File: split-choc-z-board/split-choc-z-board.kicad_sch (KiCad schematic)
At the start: 44 parts, among them J1 AudioJack4_Ground, SW1 SW_SPST, SW10 SW_SPST, SW11 SW_SPST, SW12 SW_SPST, SW13 SW_SPST, SW14 SW_SPST, SW15 SW_SPST, SW16 SW_SPST, SW17 SW_SPST, SW18 SW_SPST, SW2 SW_SPST, SW3 SW_SPST, SW4 SW_SPST, SW5 SW_SPST, SW6 SW_SPST, SW7 SW_SPST, SW8 SW_SPST, SW9 SW_SPST

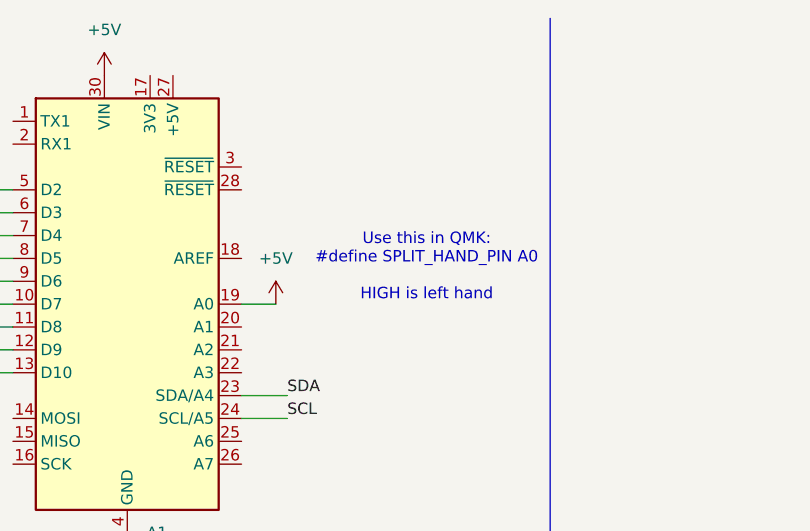
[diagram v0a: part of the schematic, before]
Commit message: Refactored schematic and added footprint library
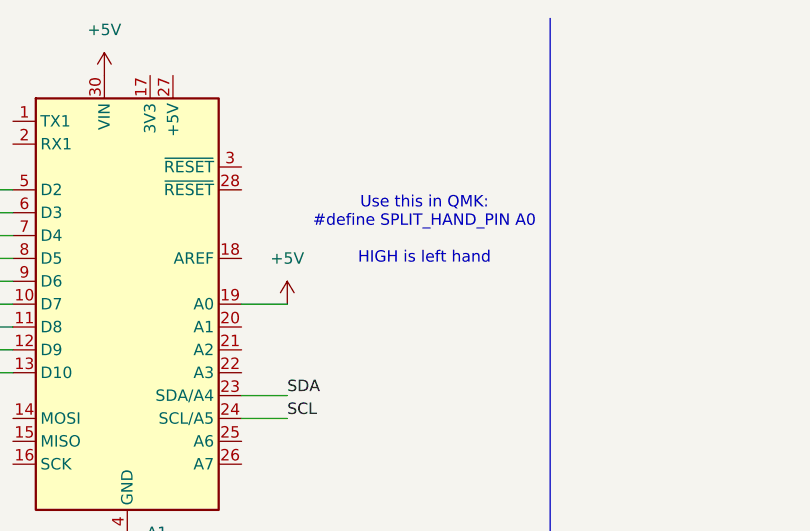
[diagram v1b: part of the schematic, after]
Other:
- title: (none) -> Split Choc Z Board Master Layout
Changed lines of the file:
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@@
 	(generator_version "9.0")
 	(paper "A4")
+	(title_block
+		(title "Split Choc Z Board Master Layout")
+		(date "2025-05-07")
+		(rev "1")
+	)
 	(text "Use this in QMK: \n#define SPLIT_HAND_PIN A0\n\nHIGH is left hand"
 		(exclude_from_sim no)
-		(at 113.284 40.386 0)
+		(at 113.03 36.322 0)
 		(effects
 			(font
@@
 	(wire
 		(pts
-			(xy 92.71 44.45) (xy 96.52 44.45)
-		)
-		(stroke
-			(width 0)
-			(type default)
-		)
-	)
-	(wire
-		(pts
 			(xy 64.77 44.45) (xy 67.31 44.45)
 		)
@@
 	(wire
 		(pts
+			(xy 92.71 44.45) (xy 97.79 44.45)
+		)
+		(stroke
+			(width 0)
+			(type default)
+		)
+	)
+	(wire
+		(pts
 			(xy 231.14 139.7) (xy 205.74 139.7)
 		)
@@
 	(symbol
 		(lib_id "power:+5V")
-		(at 96.52 44.45 0)
+		(at 97.79 44.45 0)
 		(unit 1)
 		(exclude_from_sim no)
@@
 		(dnp no)
 		(fields_autoplaced yes)
-		(property "Reference" "#PWR012"
-			(at 96.52 48.26 0)
+		(property "Reference" "#PWR014"
+			(at 97.79 48.26 0)
 			(effects
 				(font
@@
 		)
 		(property "Value" "+5V"
-			(at 96.52 39.37 0)
+			(at 97.79 39.37 0)
 			(effects
 				(font
@@
 		)
 		(property "Footprint" ""
-			(at 96.52 44.45 0)
+			(at 97.79 44.45 0)
 			(effects
 				(font
@@
 		)
 		(property "Datasheet" ""
-			(at 96.52 44.45 0)
+			(at 97.79 44.45 0)
 			(effects
 				(font
@@
 		)
 		(property "Description" "Power symbol creates a global label with name \"+5V\""
-			(at 96.52 44.45 0)
+			(at 97.79 44.45 0)
 			(effects
 				(font
@@
 			(project "split-choc-z-board"
 				(path "/ed5781c6-5e97-451b-a423-3f437c76b176"
-					(reference "#PWR012")
+					(reference "#PWR014")
 					(unit 1)
 				)

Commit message: Added more footprints to symbols and started placement
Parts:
- D1, D10, D11, D12, D13, D14, D15, D16, D17, D18, D2, D3, D4, D5, D6, D7, D8, D9: footprint (none) -> Diode_THT:D_DO-35_SOD27_P7.62mm_Horizontal
- R1, R2, R3, R4, R5, R6: footprint (none) -> Resistor_THT:R_Axial_DIN0207_L6.3mm_D2.5mm_P10.16mm_Horizontal
- SW1, SW10, SW11, SW12, SW13, SW14, SW15, SW16, SW17, SW18, SW2, SW3, SW4, SW5, SW6, SW7, SW8, SW9: footprint (none) -> ScottoKeebs_Choc:Choc_V2_1.00u
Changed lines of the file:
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@@
 			)
 		)
-		(property "Footprint" ""
+		(property "Footprint" "Resistor_THT:R_Axial_DIN0207_L6.3mm_D2.5mm_P10.16mm_Horizontal"
 			(at 221.742 34.29 90)
 			(effects
@@
 			)
 		)
-		(property "Footprint" ""
+		(property "Footprint" "ScottoKeebs_Choc:Choc_V2_1.00u"
 			(at 269.24 78.74 0)
 			(effects
@@
 			)
 		)
-		(property "Footprint" ""
+		(property "Footprint" "Diode_THT:D_DO-35_SOD27_P7.62mm_Horizontal"
 			(at 260.35 78.74 0)
 			(effects
@@
 			)
 		)
-		(property "Footprint" ""
+		(property "Footprint" "ScottoKeebs_Choc:Choc_V2_1.00u"
 			(at 218.44 53.34 0)
 			(effects
@@
 			)
 		)
-		(property "Footprint" ""
+		(property "Footprint" "ScottoKeebs_Choc:Choc_V2_1.00u"
 			(at 243.84 78.74 0)
 			(effects
@@
 			)
 		)
-		(property "Footprint" ""
+		(property "Footprint" "Diode_THT:D_DO-35_SOD27_P7.62mm_Horizontal"
 			(at 234.95 78.74 0)
 			(effects
@@
 			)
 		)
-		(property "Footprint" ""
+		(property "Footprint" "ScottoKeebs_Choc:Choc_V2_1.00u"
 			(at 243.84 154.94 0)
 			(effects
@@
 			)
 		)
-		(property "Footprint" ""
+		(property "Footprint" "ScottoKeebs_Choc:Choc_V2_1.00u"
 			(at 218.44 154.94 0)
 			(effects
@@
 			)
 		)
-		(property "Footprint" ""
+		(property "Footprint" "ScottoKeebs_Choc:Choc_V2_1.00u"
 			(at 193.04 53.34 0)
 			(effects
@@
 			)
 		)
-		(property "Footprint" ""
+		(property "Footprint" "Resistor_THT:R_Axial_DIN0207_L6.3mm_D2.5mm_P10.16mm_Horizontal"
 			(at 39.37 25.908 90)
 			(effects
@@
 			)
 		)
-		(property "Footprint" ""
+		(property "Footprint" "ScottoKeebs_Choc:Choc_V2_1.00u"
 			(at 269.24 129.54 0)
 			(effects
@@
 			)
 		)
-		(property "Footprint" ""
+		(property "Footprint" "ScottoKeebs_Choc:Choc_V2_1.00u"
 			(at 218.44 78.74 0)
 			(effects
@@
 			)
 		)
-		(property "Footprint" ""
+		(property "Footprint" "ScottoKeebs_Choc:Choc_V2_1.00u"
 			(at 193.04 78.74 0)
 			(effects
@@
 			)
 		)
-		(property "Footprint" ""
+		(property "Footprint" "Diode_THT:D_DO-35_SOD27_P7.62mm_Horizontal"
 			(at 260.35 104.14 0)
 			(effects
@@
 			)
 		)
-		(property "Footprint" ""
+		(property "Footprint" "Diode_THT:D_DO-35_SOD27_P7.62mm_Horizontal"
 			(at 209.55 104.14 0)
 			(effects
@@
 			)
 		)
-		(property "Footprint" ""
+		(property "Footprint" "ScottoKeebs_Choc:Choc_V2_1.00u"
 			(at 269.24 53.34 0)
 			(effects
@@
 			)
 		)
-		(property "Footprint" ""
+		(property "Footprint" "ScottoKeebs_Choc:Choc_V2_1.00u"
 			(at 243.84 53.34 0)
 			(effects
@@
 			)
 		)
-		(property "Footprint" ""
+		(property "Footprint" "Diode_THT:D_DO-35_SOD27_P7.62mm_Horizontal"
 			(at 184.15 53.34 0)
 			(effects
@@
 			)
 		)
-		(property "Footprint" ""
+		(property "Footprint" "Diode_THT:D_DO-35_SOD27_P7.62mm_Horizontal"
 			(at 260.35 53.34 0)
 			(effects
@@
 			)
 		)
-		(property "Footprint" ""
+		(property "Footprint" "Diode_THT:D_DO-35_SOD27_P7.62mm_Horizontal"
 			(at 234.95 154.94 0)
 			(effects
@@
 			)
 		)
-		(property "Footprint" ""
+		(property "Footprint" "ScottoKeebs_Choc:Choc_V2_1.00u"
 			(at 269.24 104.14 0)
 			(effects
@@
 			)
 		)
-		(property "Footprint" ""
+		(property "Footprint" "Diode_THT:D_DO-35_SOD27_P7.62mm_Horizontal"
 			(at 260.35 129.54 0)
 			(effects
@@
 			)
 		)
-		(property "Footprint" ""
+		(property "Footprint" "Resistor_THT:R_Axial_DIN0207_L6.3mm_D2.5mm_P10.16mm_Horizontal"
 			(at 196.342 34.29 90)
 			(effects
@@
 			)
 		)
-		(property "Footprint" ""
+		(property "Footprint" "Diode_THT:D_DO-35_SOD27_P7.62mm_Horizontal"
 			(at 184.15 129.54 0)
 			(effects
@@
 			)
 		)
-		(property "Footprint" ""
+		(property "Footprint" "Diode_THT:D_DO-35_SOD27_P7.62mm_Horizontal"
 			(at 209.55 53.34 0)
 			(effects
@@
 			)
 		)
-		(property "Footprint" ""
+		(property "Footprint" "Diode_THT:D_DO-35_SOD27_P7.62mm_Horizontal"
 			(at 234.95 104.14 0)
 			(effects
@@
 			)
 		)
-		(property "Footprint" ""
+		(property "Footprint" "Resistor_THT:R_Axial_DIN0207_L6.3mm_D2.5mm_P10.16mm_Horizontal"
 			(at 24.13 25.908 90)
 			(effects
@@
 			)
 		)
-		(property "Footprint" ""
+		(property "Footprint" "ScottoKeebs_Choc:Choc_V2_1.00u"
 			(at 193.04 104.14 0)
 			(effects
@@
 			)
 		)
-		(property "Footprint" ""
+		(property "Footprint" "Diode_THT:D_DO-35_SOD27_P7.62mm_Horizontal"
 			(at 184.15 104.14 0)
 			(effects
@@
 			)
 		)
-		(property "Footprint" ""
+		(property "Footprint" "Diode_THT:D_DO-35_SOD27_P7.62mm_Horizontal"
 			(at 234.95 129.54 0)
 			(effects
@@
 			)
 		)
-		(property "Footprint" ""
+		(property "Footprint" "Resistor_THT:R_Axial_DIN0207_L6.3mm_D2.5mm_P10.16mm_Horizontal"
 			(at 272.542 34.29 90)
 			(effects
@@
 			)
 		)
-		(property "Footprint" ""
+		(property "Footprint" "Resistor_THT:R_Axial_DIN0207_L6.3mm_D2.5mm_P10.16mm_Horizontal"
 			(at 247.142 34.29 90)
 			(effects
@@
 			)
 		)
-		(property "Footprint" ""
+		(property "Footprint" "Diode_THT:D_DO-35_SOD27_P7.62mm_Horizontal"
 			(at 209.55 78.74 0)
 			(effects
@@
 			)
 		)
-		(property "Footprint" ""
+		(property "Footprint" "ScottoKeebs_Choc:Choc_V2_1.00u"
 			(at 243.84 104.14 0)
 			(effects
@@
 			)
 		)
-		(property "Footprint" ""
+		(property "Footprint" "Diode_THT:D_DO-35_SOD27_P7.62mm_Horizontal"
 			(at 184.15 78.74 0)
 			(effects
@@
 			)
 		)
-		(property "Footprint" ""
+		(property "Footprint" "Diode_THT:D_DO-35_SOD27_P7.62mm_Horizontal"
 			(at 209.55 129.54 0)
 			(effects
@@
 			)
 		)
-		(property "Footprint" ""
+		(property "Footprint" "ScottoKeebs_Choc:Choc_V2_1.00u"
 			(at 193.04 129.54 0)
 			(effects
@@
 			)
 		)
-		(property "Footprint" ""
+		(property "Footprint" "ScottoKeebs_Choc:Choc_V2_1.00u"
 			(at 243.84 129.54 0)
 			(effects
@@
 			)
 		)
-		(property "Footprint" ""
+		(property "Footprint" "Diode_THT:D_DO-35_SOD27_P7.62mm_Horizontal"
 			(at 234.95 53.34 0)
 			(effects
@@
 			)
 		)
-		(property "Footprint" ""
+		(property "Footprint" "Diode_THT:D_DO-35_SOD27_P7.62mm_Horizontal"
 			(at 209.55 154.94 0)
 			(effects
@@
 			)
 		)
-		(property "Footprint" ""
+		(property "Footprint" "ScottoKeebs_Choc:Choc_V2_1.00u"
 			(at 218.44 104.14 0)
 			(effects
@@
 			)
 		)
-		(property "Footprint" ""
+		(property "Footprint" "ScottoKeebs_Choc:Choc_V2_1.00u"
 			(at 218.44 129.54 0)
 			(effects

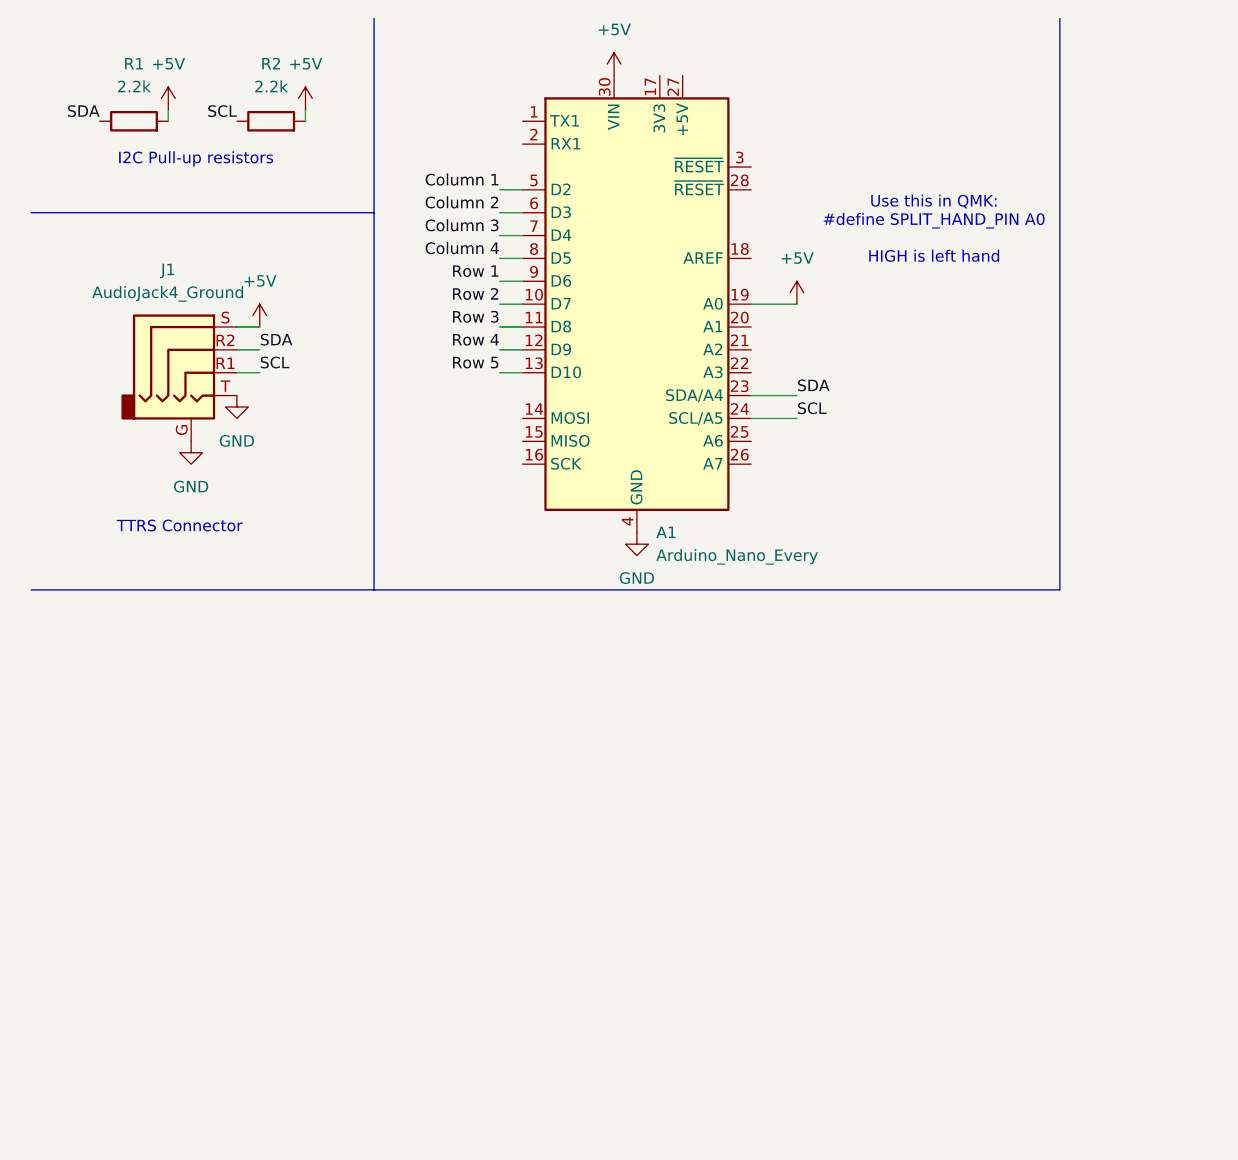
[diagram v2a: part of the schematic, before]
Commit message: Changed TTRS to USB C
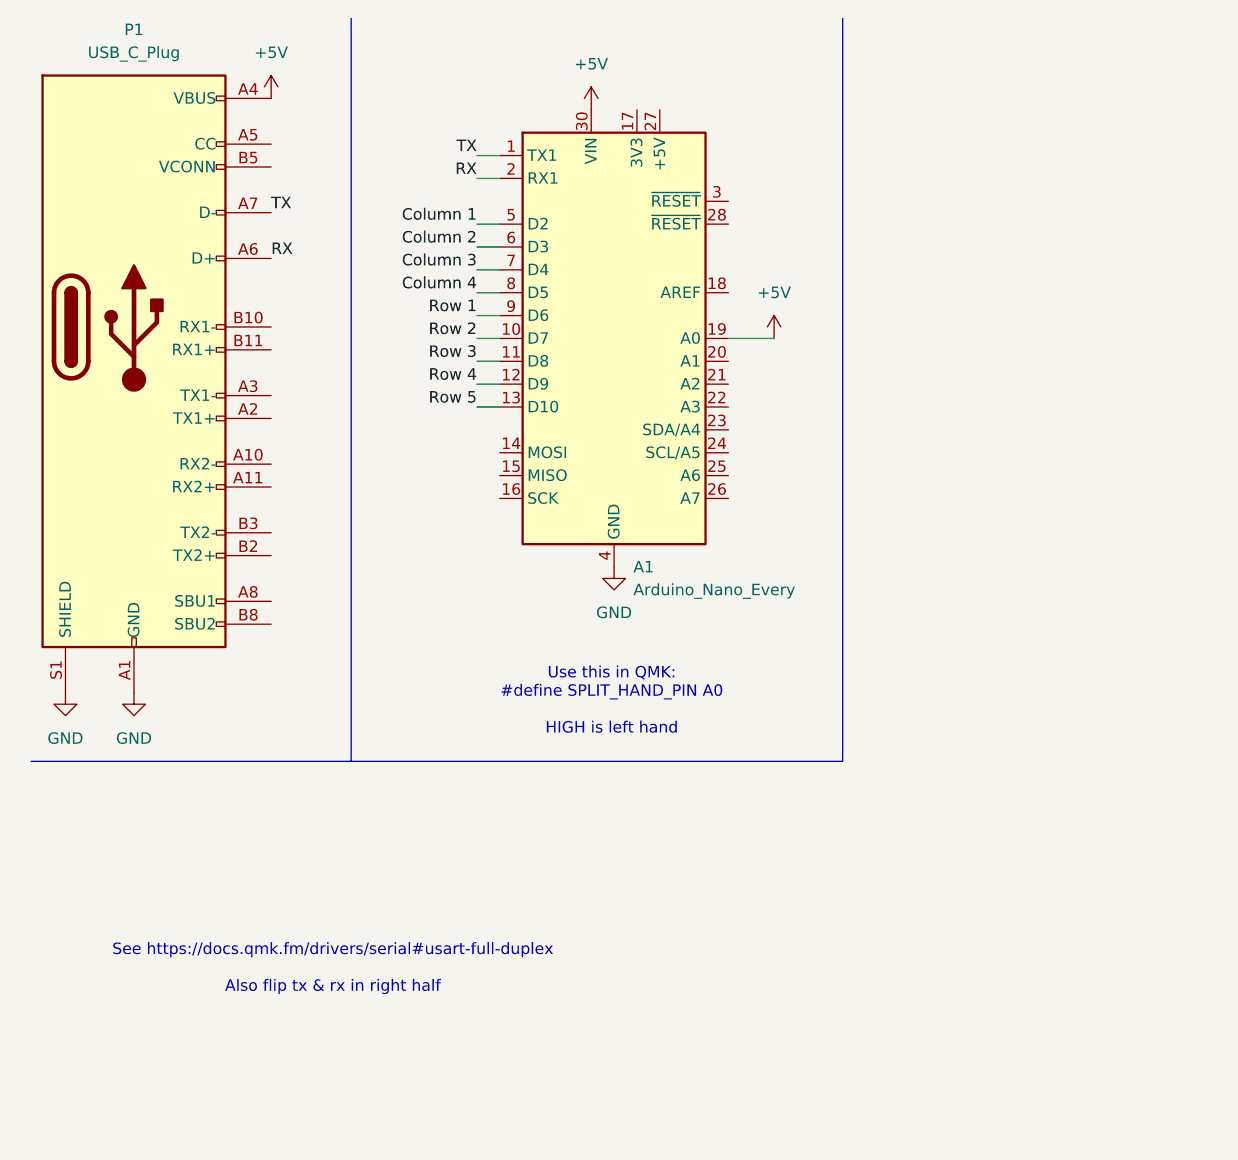
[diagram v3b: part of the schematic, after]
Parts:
- removed J1: AudioJack4_Ground, symbol Connector_Audio:AudioJack4_Ground
- removed R1, R2: 2.2k, Resistor_THT:R_Axial_DIN0207_L6.3mm_D2.5mm_P10.16mm_Horizontal, symbol Device:R
- added P1: USB_C_Plug, symbol Connector:USB_C_Plug
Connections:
- net +5V: now also P1.A4 (VBUS), P1.A9 (VBUS), P1.B4 (VBUS), P1.B9 (VBUS)
- net GND: now also P1.A1 (GND), P1.A12 (GND), P1.B1 (GND), P1.B12 (GND), P1.S1 (SHIELD)
- net TX: now reaches A1.1 (TX1)
- net TX: now also P1.A7 (D-)
- net RX: now reaches A1.2 (RX1)
- net RX: now also P1.A6 (D+)
- net SCL: no longer names the net of A1.24 (SCL/A5)
- net SDA: no longer names the net of A1.23 (SDA/A4)
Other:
- note added: "See https://docs.qmk.fm/drivers/serial#usart-full-duplex Also flip tx & rx in right half"
- note removed: "I2C Pull-up resistors"
- note removed: "TTRS Connector"
- moved on the sheet: A1
